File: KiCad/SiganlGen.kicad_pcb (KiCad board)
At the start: 2 copper layers, 96.5 x 67.3 mm, 90 parts, among them J1 Barrel_Jack_MountingPin, J2 Conn_Coaxial, J3 LCD_Conn, J4 Enc_Conn, J6 Btn&Led, J7 PWR, J9 Btn_Matrix, Q1 BD135, Q2 BD136, U1 RaspberryPi_Pico, U2 MC34063AP, U3 LM7805_TO220, U4 LM337_TO220, U6 LM318H, U7 LM317_TO-220

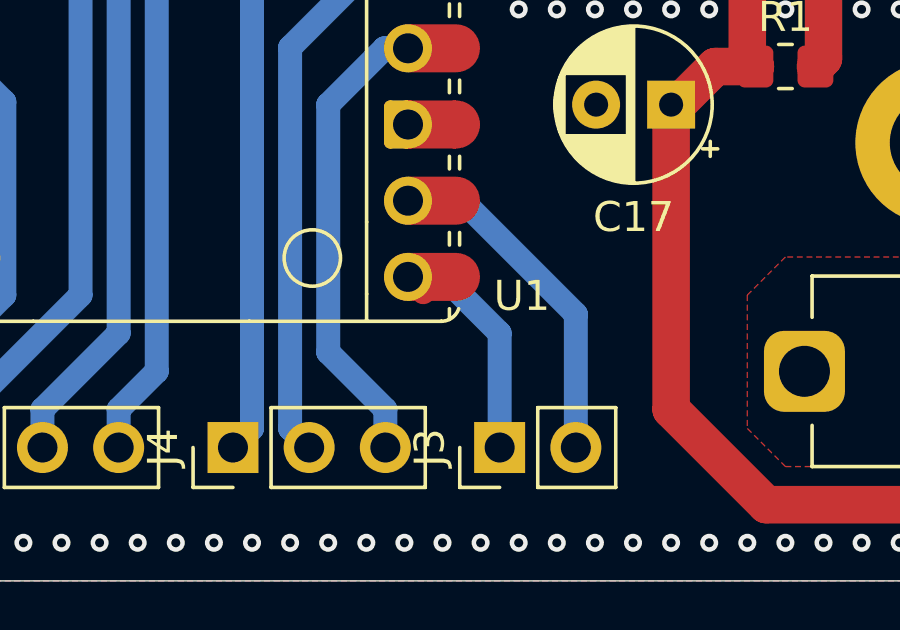
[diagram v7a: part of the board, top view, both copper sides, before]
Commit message: output sim, filter sim, filter sch, output change
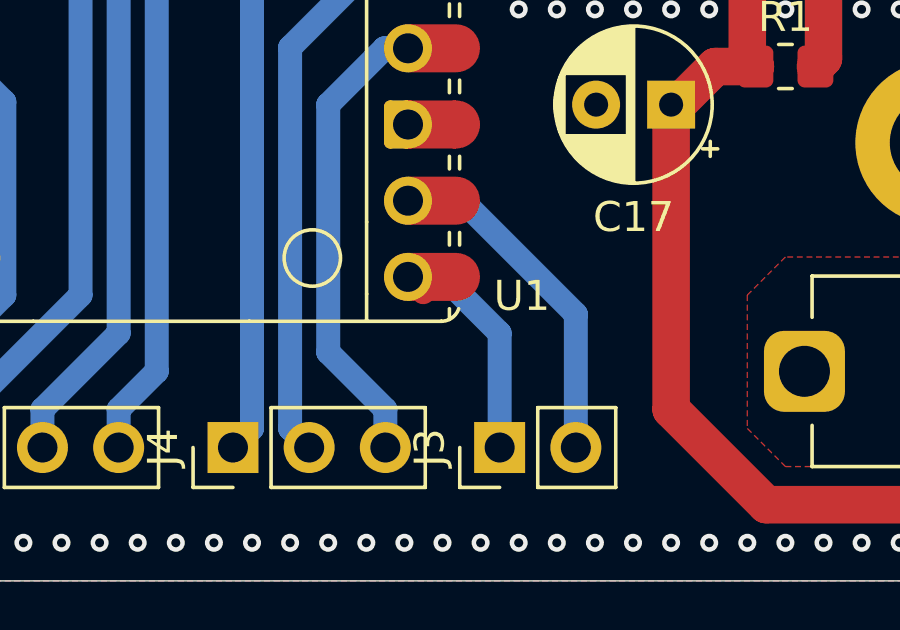
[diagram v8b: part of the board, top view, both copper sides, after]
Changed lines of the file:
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@@
 		(fp_arc
 			(start 10.579676 25.189937)
-			(mid 10.35796 25.493961)
+			(mid 10.357946 25.493957)
 			(end 10 25.61)
 			(stroke
@@
 		(tags "resistor handsolder")
 		(property "Reference" "R40"
-			(at 0 -1.65 360)
+			(at 0 -1.65 0)
 			(layer "F.SilkS")
 			(effects
@@
 		)
 		(property "Value" "100"
-			(at 0 1.65 360)
+			(at 0 1.65 0)
 			(layer "F.Fab")
 			(effects
@@
 		)
 		(fp_text user "${REFERENCE}"
-			(at 0 0 360)
+			(at 0 0 0)
 			(layer "F.Fab")
 			(effects
@@
 		(tags "resistor handsolder")
 		(property "Reference" "R5"
-			(at 0 1.65 270)
+			(at 0 1.65 -90)
 			(layer "B.SilkS")
 			(effects
@@
 		)
 		(property "Value" "100"
-			(at 0 -1.65 270)
+			(at 0 -1.65 -90)
 			(layer "B.Fab")
 			(effects
@@
 		)
 		(fp_text user "${REFERENCE}"
-			(at 0 0 270)
+			(at 0 0 -90)
 			(layer "B.Fab")
 			(effects
@@
 		(tags "D_SOD-123F")
 		(property "Reference" "D2"
-			(at -0.127 1.905 270)
+			(at -0.127 1.905 -90)
 			(layer "B.SilkS")
 			(effects
@@
 		)
 		(property "Value" "1N4007"
-			(at 0 -2.1 270)
+			(at 0 -2.1 -90)
 			(layer "B.Fab")
 			(hide yes)
@@
 		)
 		(fp_text user "${REFERENCE}"
-			(at -0.127 1.905 270)
+			(at -0.127 1.905 -90)
 			(layer "B.Fab")
 			(effects
@@
 		(tags "resistor handsolder")
 		(property "Reference" "R3"
-			(at -0.762 1.65 360)
+			(at -0.762 1.65 0)
 			(layer "B.SilkS")
 			(effects
@@
 		)
 		(property "Value" "14k"
-			(at 0 -1.65 360)
+			(at 0 -1.65 0)
 			(layer "B.Fab")
 			(effects
@@
 		)
 		(fp_text user "${REFERENCE}"
-			(at 0 0 360)
+			(at 0 0 0)
 			(layer "B.Fab")
 			(effects
@@
 		(tags "capacitor handsolder")
 		(property "Reference" "C19"
-			(at 0 1.68 360)
+			(at 0 1.68 0)
 			(layer "B.SilkS")
 			(effects
@@
 		)
 		(property "Value" "100n"
-			(at 0 -1.68 360)
+			(at 0 -1.68 0)
 			(layer "B.Fab")
 			(effects
@@
 		)
 		(fp_text user "${REFERENCE}"
-			(at 0 0 360)
+			(at 0 0 0)
 			(layer "B.Fab")
 			(effects
